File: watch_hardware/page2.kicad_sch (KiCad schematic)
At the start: 36 parts, among them J2 TF_Card, Q1 PMOS, U7 LPS22HB, U8 CJC4344H, U9 OPA2192

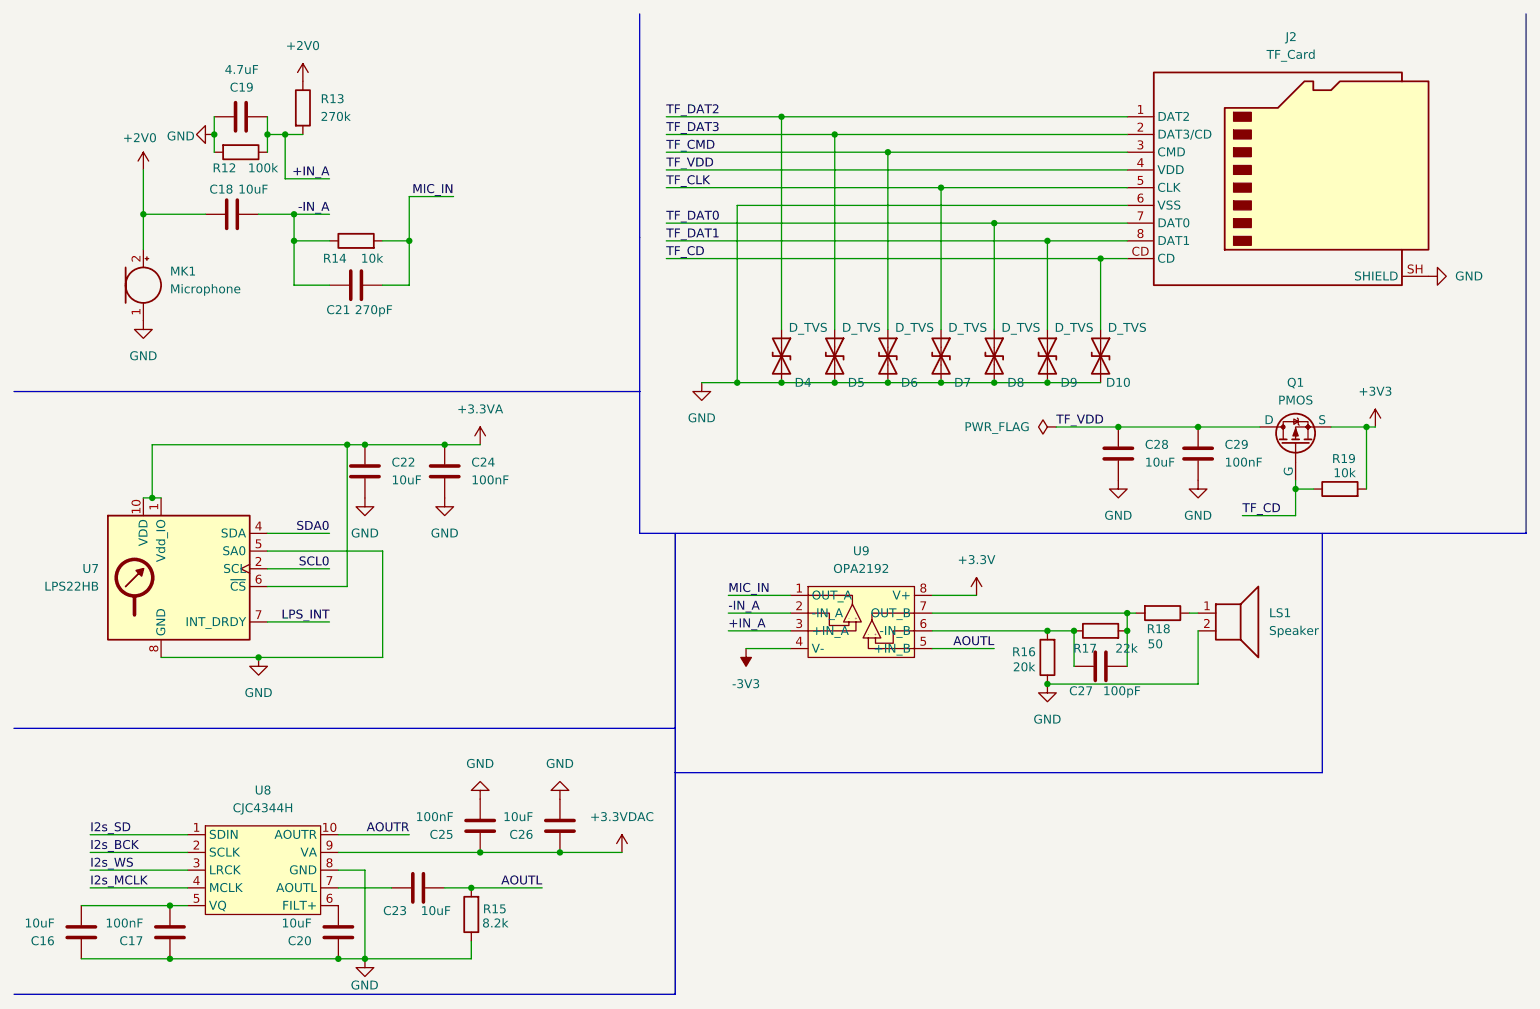
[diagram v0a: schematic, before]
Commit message: 准备添加卫星定位
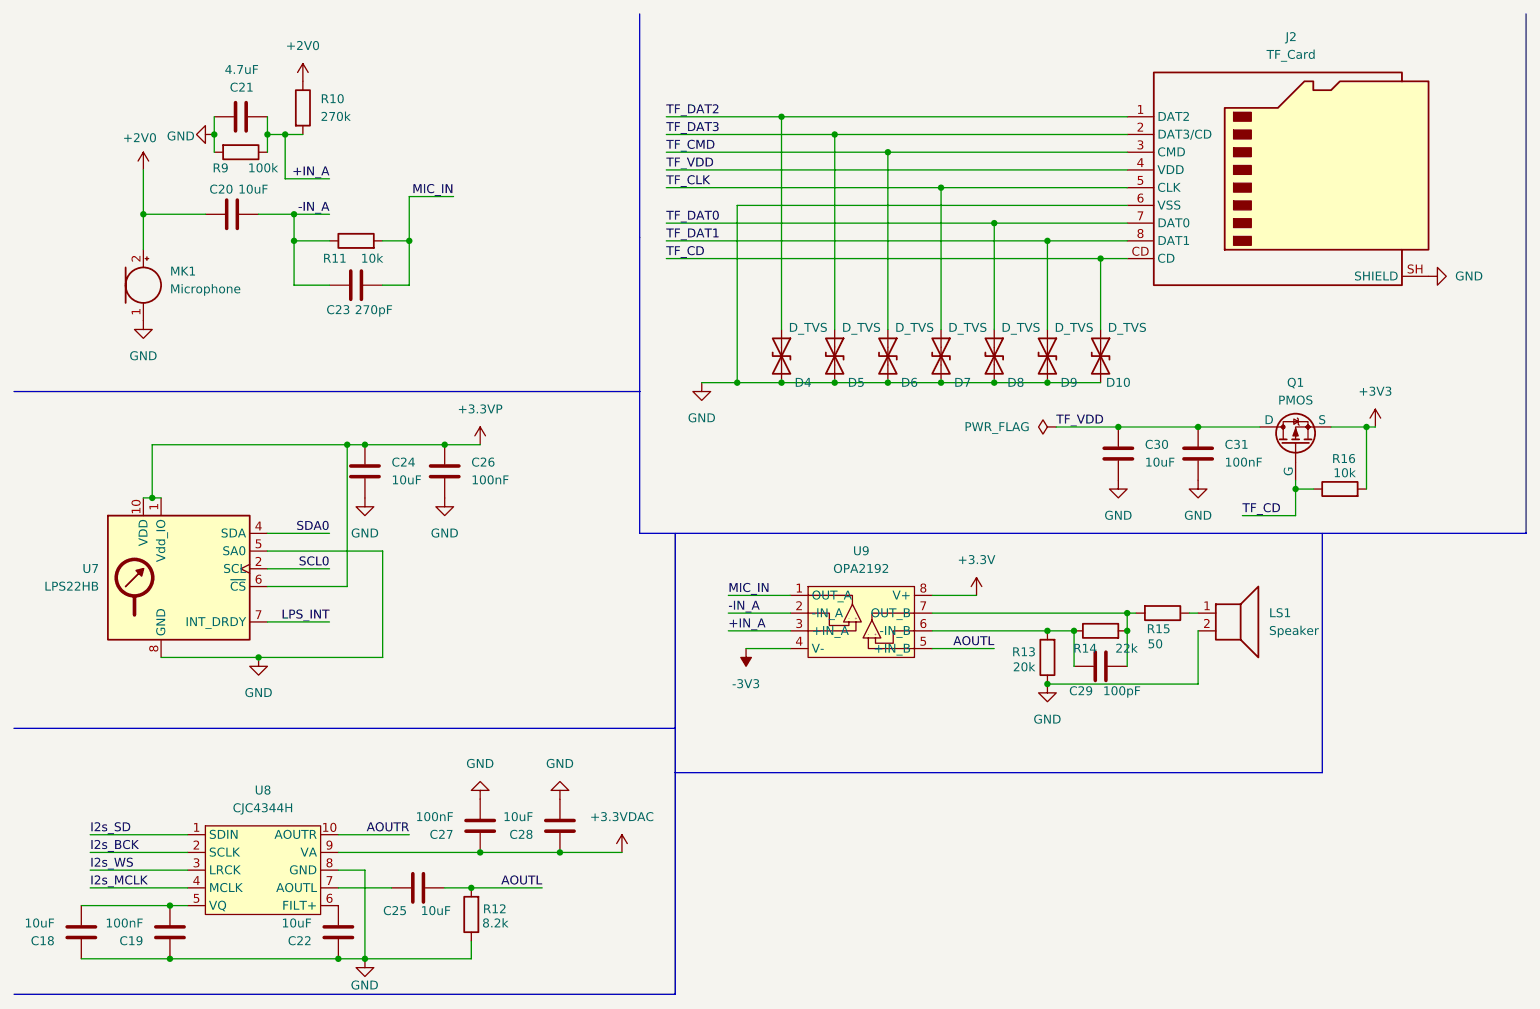
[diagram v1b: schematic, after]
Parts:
- renumbered C16 to C18, C17 to C19, C18 to C20, C19 to C21, C20 to C22, C21 to C23, C22 to C24, C23 to C25, C24 to C26, C25 to C27, C26 to C28, C27 to C29, C28 to C30, C29 to C31, R13 to R10, R14 to R11, R15 to R12, R16 to R13, R17 to R14, R18 to R15, R19 to R16, R12 to R9
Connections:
- net +3.3VA renamed +3.3VP
